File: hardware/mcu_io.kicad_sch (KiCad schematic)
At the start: 23 parts, among them J4 SWD, U10 74HC595D, U11 74HC595D, U12 74HC595D, U13 74HC595D, U6 74HC165D, U7 74HC165D, U8 74HC165D, U9 74HC165D

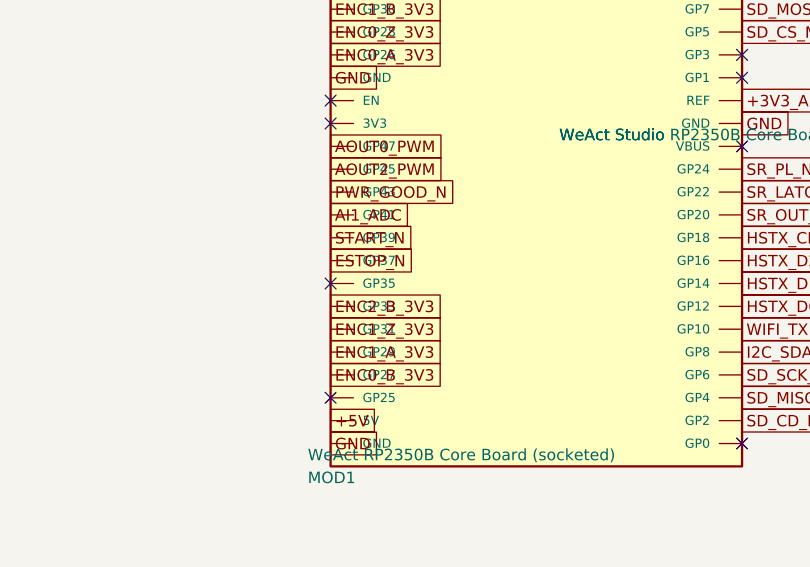
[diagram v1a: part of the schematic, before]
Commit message: Update RP2350 board power and I/O design
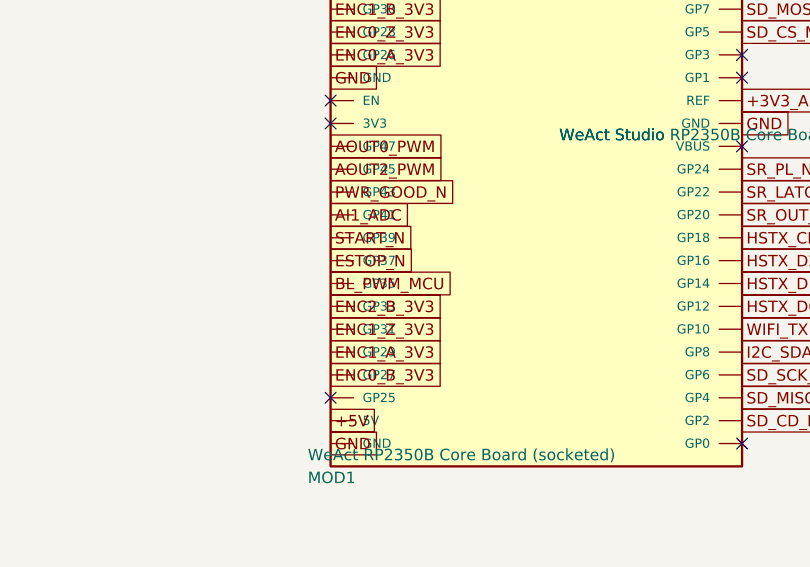
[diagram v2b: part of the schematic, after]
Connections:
- net BL_PWM_MCU: now reaches MOD1.25 (GP35)
- no-connect marks 17 -> 16
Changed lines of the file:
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@@
 		(instances
 			(project "MCU, shift chains and safety"
-				(path "/75c4b43e-1edc-48d3-8217-1213416fdce8"
+				(path "/f6d11e54-d6a0-4701-af3d-5d8ebcd9da6c"
 					(reference "MOD1")
 					(unit 1)
@@
 		(instances
 			(project "MCU, shift chains and safety"
-				(path "/75c4b43e-1edc-48d3-8217-1213416fdce8"
+				(path "/f6d11e54-d6a0-4701-af3d-5d8ebcd9da6c"
 					(reference "J4")
 					(unit 1)
@@
 		(instances
 			(project "MCU, shift chains and safety"
-				(path "/75c4b43e-1edc-48d3-8217-1213416fdce8"
+				(path "/f6d11e54-d6a0-4701-af3d-5d8ebcd9da6c"
 					(reference "U6")
 					(unit 1)
@@
 		(instances
 			(project "MCU, shift chains and safety"
-				(path "/75c4b43e-1edc-48d3-8217-1213416fdce8"
+				(path "/f6d11e54-d6a0-4701-af3d-5d8ebcd9da6c"
 					(reference "C22")
 					(unit 1)
@@
 		(instances
 			(project "MCU, shift chains and safety"
-				(path "/75c4b43e-1edc-48d3-8217-1213416fdce8"
+				(path "/f6d11e54-d6a0-4701-af3d-5d8ebcd9da6c"
 					(reference "U7")
 					(unit 1)
@@
 		(instances
 			(project "MCU, shift chains and safety"
-				(path "/75c4b43e-1edc-48d3-8217-1213416fdce8"
+				(path "/f6d11e54-d6a0-4701-af3d-5d8ebcd9da6c"
 					(reference "C23")
 					(unit 1)
@@
 		(instances
 			(project "MCU, shift chains and safety"
-				(path "/75c4b43e-1edc-48d3-8217-1213416fdce8"
+				(path "/f6d11e54-d6a0-4701-af3d-5d8ebcd9da6c"
 					(reference "U8")
 					(unit 1)
@@
 		(instances
 			(project "MCU, shift chains and safety"
-				(path "/75c4b43e-1edc-48d3-8217-1213416fdce8"
+				(path "/f6d11e54-d6a0-4701-af3d-5d8ebcd9da6c"
 					(reference "C24")
 					(unit 1)
@@
 		(instances
 			(project "MCU, shift chains and safety"
-				(path "/75c4b43e-1edc-48d3-8217-1213416fdce8"
+				(path "/f6d11e54-d6a0-4701-af3d-5d8ebcd9da6c"
 					(reference "U9")
 					(unit 1)
@@
 		(instances
 			(project "MCU, shift chains and safety"
-				(path "/75c4b43e-1edc-48d3-8217-1213416fdce8"
+				(path "/f6d11e54-d6a0-4701-af3d-5d8ebcd9da6c"
 					(reference "C25")
 					(unit 1)
@@
 		(instances
 			(project "MCU, shift chains and safety"
-				(path "/75c4b43e-1edc-48d3-8217-1213416fdce8"
+				(path "/f6d11e54-d6a0-4701-af3d-5d8ebcd9da6c"
 					(reference "R9")
 					(unit 1)
@@
 		(instances
 			(project "MCU, shift chains and safety"
-				(path "/75c4b43e-1edc-48d3-8217-1213416fdce8"
+				(path "/f6d11e54-d6a0-4701-af3d-5d8ebcd9da6c"
 					(reference "R10")
 					(unit 1)
@@
 		(instances
 			(project "MCU, shift chains and safety"
-				(path "/75c4b43e-1edc-48d3-8217-1213416fdce8"
+				(path "/f6d11e54-d6a0-4701-af3d-5d8ebcd9da6c"
 					(reference "R11")
 					(unit 1)
@@
 		(instances
 			(project "MCU, shift chains and safety"
-				(path "/75c4b43e-1edc-48d3-8217-1213416fdce8"
+				(path "/f6d11e54-d6a0-4701-af3d-5d8ebcd9da6c"
 					(reference "U10")
 					(unit 1)
@@
 		(instances
 			(project "MCU, shift chains and safety"
-				(path "/75c4b43e-1edc-48d3-8217-1213416fdce8"
+				(path "/f6d11e54-d6a0-4701-af3d-5d8ebcd9da6c"
 					(reference "C26")
 					(unit 1)
@@
 		(instances
 			(project "MCU, shift chains and safety"
-				(path "/75c4b43e-1edc-48d3-8217-1213416fdce8"
+				(path "/f6d11e54-d6a0-4701-af3d-5d8ebcd9da6c"
 					(reference "U11")
 					(unit 1)
@@
 		(instances
 			(project "MCU, shift chains and safety"
-				(path "/75c4b43e-1edc-48d3-8217-1213416fdce8"
+				(path "/f6d11e54-d6a0-4701-af3d-5d8ebcd9da6c"
 					(reference "C27")
 					(unit 1)
@@
 		(instances
 			(project "MCU, shift chains and safety"
-				(path "/75c4b43e-1edc-48d3-8217-1213416fdce8"
+				(path "/f6d11e54-d6a0-4701-af3d-5d8ebcd9da6c"
 					(reference "U12")
 					(unit 1)
@@
 		(instances
 			(project "MCU, shift chains and safety"
-				(path "/75c4b43e-1edc-48d3-8217-1213416fdce8"
+				(path "/f6d11e54-d6a0-4701-af3d-5d8ebcd9da6c"
 					(reference "C28")
 					(unit 1)
@@
 		(instances
 			(project "MCU, shift chains and safety"
-				(path "/75c4b43e-1edc-48d3-8217-1213416fdce8"
+				(path "/f6d11e54-d6a0-4701-af3d-5d8ebcd9da6c"
 					(reference "U13")
 					(unit 1)
@@
 		(instances
 			(project "MCU, shift chains and safety"
-				(path "/75c4b43e-1edc-48d3-8217-1213416fdce8"
+				(path "/f6d11e54-d6a0-4701-af3d-5d8ebcd9da6c"
 					(reference "C29")
 					(unit 1)
@@
 		(instances
 			(project "MCU, shift chains and safety"
-				(path "/75c4b43e-1edc-48d3-8217-1213416fdce8"
+				(path "/f6d11e54-d6a0-4701-af3d-5d8ebcd9da6c"
 					(reference "R12")
 					(unit 1)
@@
 		(instances
 			(project "MCU, shift chains and safety"
-				(path "/75c4b43e-1edc-48d3-8217-1213416fdce8"
+				(path "/f6d11e54-d6a0-4701-af3d-5d8ebcd9da6c"
 					(reference "R13")
 					(unit 1)
@@
 		)
 	)
+	(global_label "BL_PWM_MCU"
+		(shape passive)
+		(at 127 116.84 0.0000)
+		(fields_autoplaced yes)
+		(effects
+			(font
+				(size 1.27 1.27)
+			)
+			(justify left bottom)
+		)
+	)
 	(global_label "ENC2_B_3V3"
 		(shape passive)
@@
 	)
 	(no_connect
-		(at 127 116.84)
-	)
-	(no_connect
